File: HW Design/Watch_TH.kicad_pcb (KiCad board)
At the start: 2 copper layers, 49.6 x 66 mm, 21 parts, among them SW1 SW_SPST, U1 TDCR1050M, U2 74AHCT595, U3 L78M05ABV, U4 74AHCT595, U5 ATtiny85-20P

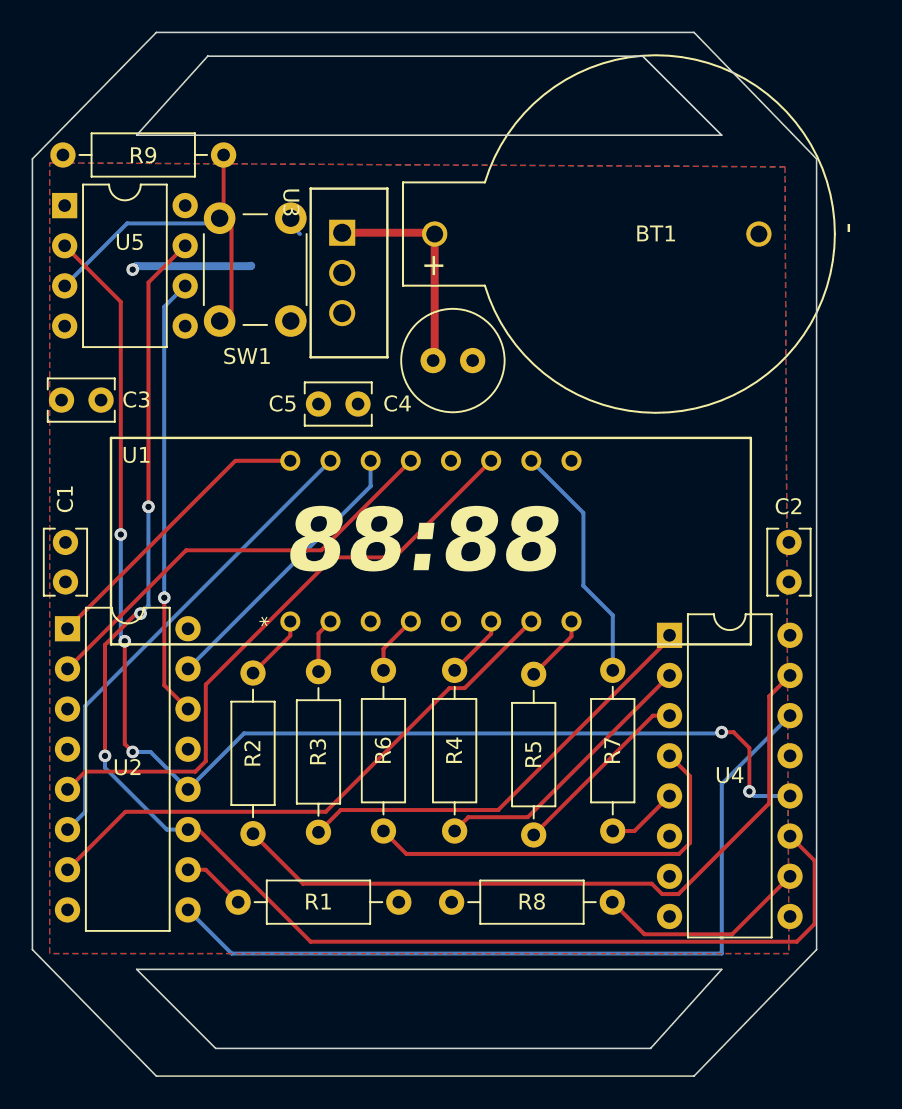
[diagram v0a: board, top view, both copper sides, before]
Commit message: HW Update
Rerouted to connect missed ratsnest lines and connected together
isolated pours

Tags:
 * Type: BugFix
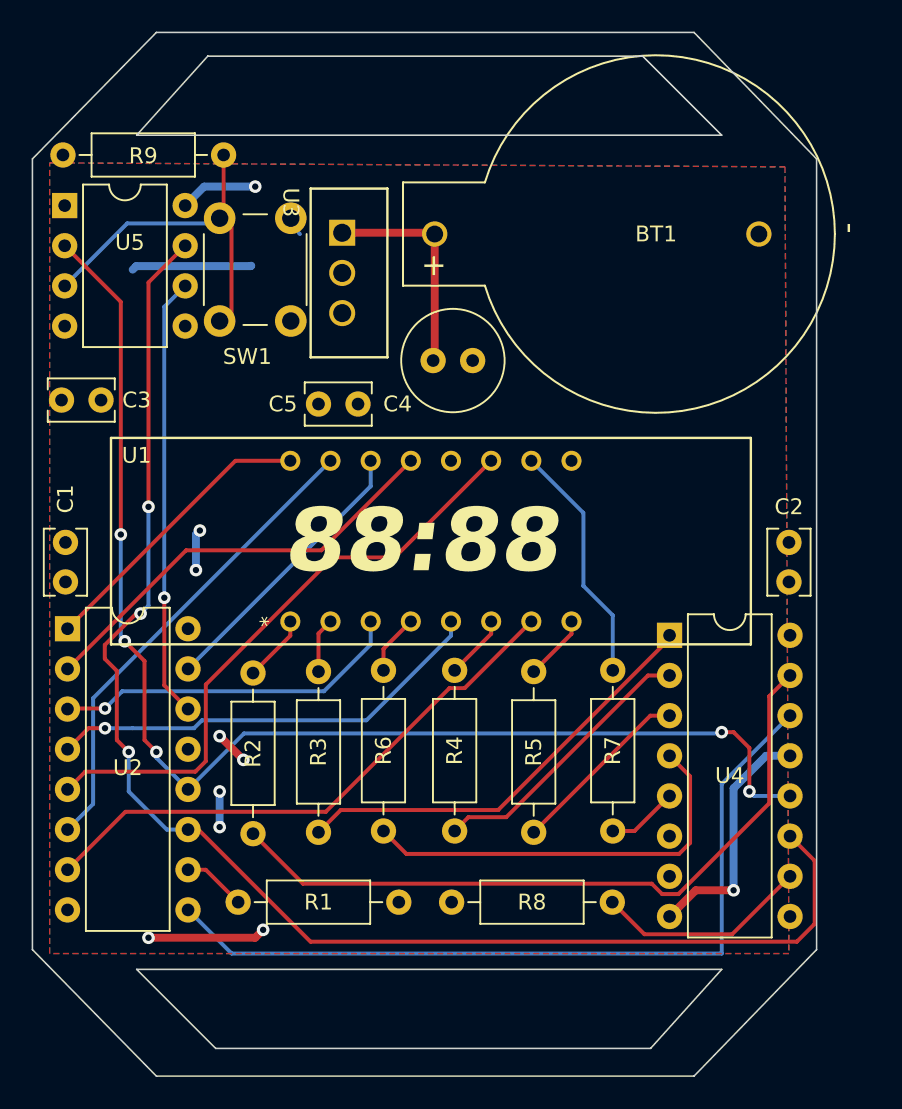
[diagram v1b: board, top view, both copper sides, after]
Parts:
- moved R5 0.17 mm to (153.9, 94.7)
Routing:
- net /LED_nE: track 0.00 -> 28.1 mm, vias 0 -> 1
- net GND: track 7.72 -> 32.9 mm, vias 1 -> 5
- net /LED_nD: track 0.00 -> 22.3 mm, vias 0 -> 1
- net +5V: track 0.00 -> 9.78 mm, vias 0 -> 5
- net /uC_RCLK: track 81.3 -> 80.6 mm
